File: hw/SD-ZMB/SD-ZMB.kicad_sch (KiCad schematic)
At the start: 0 parts

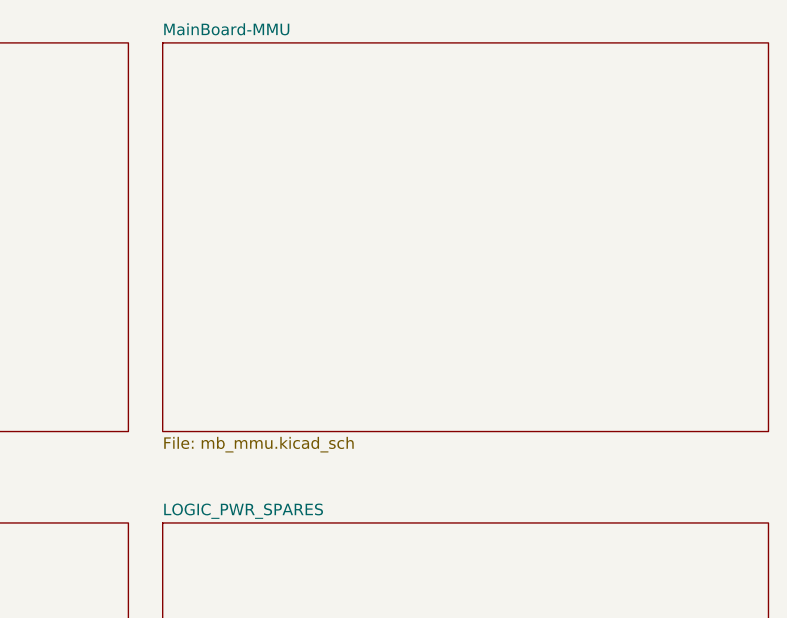
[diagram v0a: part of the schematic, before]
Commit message: HW: PR4 CPU, Memory, page cleaner.
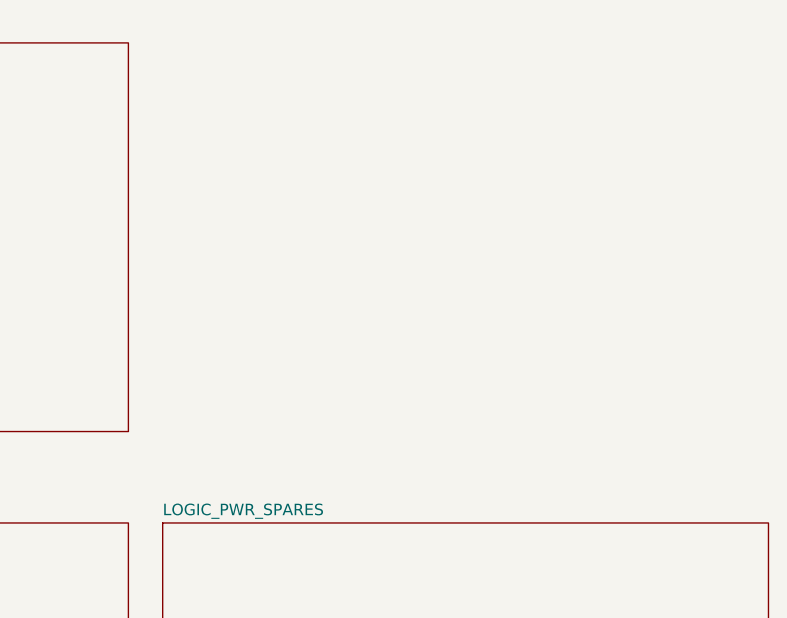
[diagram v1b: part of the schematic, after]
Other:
- removed sheet MainBoard-MMU
- title: MicroSystem Z80 w/Front Panel & RC2014 Bus -> Retro Z80 Motherboard w/Paripherals & RC2014 Bus
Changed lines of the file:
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@@
 	(paper "User" 419.1 323.85)
 	(title_block
-		(title "MicroSystem Z80 w/Front Panel & RC2014 Bus")
-		(date "2025-09-22")
-		(rev "v1.0")
+		(title "Retro Z80 Motherboard w/Paripherals & RC2014 Bus")
+		(date "2025-10-08")
+		(rev "PR4")
 		(company "SilkyDESIGN")
-		(comment 1 "Copyright 2025 AESilky")
-		(comment 3 "MicroSystem Z80 w/Front Panel & RC2014 Bus")
+		(comment 1 "Copyright 2025 AESilky & SMcCown")
 	)
 	(sheet
@@
 		)
 		(instances
-			(project "SD-MSZ"
+			(project "SD-ZMB"
 				(path "/62236e9f-ef27-467c-852b-587c32c473f1"
 					(page "2")
@@
 		)
 		(instances
-			(project "SD-MSZ"
+			(project "SD-ZMB"
 				(path "/62236e9f-ef27-467c-852b-587c32c473f1"
-					(page "5")
-				)
-			)
-		)
-	)
-	(sheet
-		(at 102.87 27.94)
-		(size 67.31 43.18)
-		(exclude_from_sim no)
-		(in_bom yes)
-		(on_board yes)
-		(dnp no)
-		(fields_autoplaced yes)
-		(stroke
-			(width 0.1524)
-			(type solid)
-		)
-		(fill
-			(color 0 0 0 0.0000)
-		)
-		(property "Sheetname" "MainBoard-MMU"
-			(at 102.87 27.2284 0)
-			(effects
-				(font
-					(size 1.27 1.27)
-				)
-				(justify left bottom)
-			)
-		)
-		(property "Sheetfile" "mb_mmu.kicad_sch"
-			(at 102.87 71.7046 0)
-			(effects
-				(font
-					(size 1.27 1.27)
-				)
-				(justify left top)
-			)
-		)
-		(instances
-			(project "SD-MSZ"
-				(path "/62236e9f-ef27-467c-852b-587c32c473f1"
-					(page "3")
+					(page "4")
 				)
 			)
@@
 		)
 		(instances
-			(project "SD-MSZ"
+			(project "SD-ZMB"
 				(path "/62236e9f-ef27-467c-852b-587c32c473f1"
-					(page "4")
+					(page "3")
 				)
 			)
